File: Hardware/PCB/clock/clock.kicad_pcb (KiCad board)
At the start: 2 copper layers, 146 x 170.5 mm, 65 parts, among them J1 AudioJack2, J2 Synth_power_2x5, J3 AudioJack2, J4 AudioJack2, J5 AudioJack2, J6 AudioJack2, J7 AudioJack2, J8 Conn_02x04_Odd_Even, J9 Conn_02x04_Odd_Even, SW1 RotaryEncoder, SW2 SW_Push, U1 40106

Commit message: pre fab updates, gerbers, schem pdf
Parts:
- added B1: Board, ao_tht:Board_Marker, F.Cu at (96.5, 42.5)
- added B2: Board, ao_tht:Board_Marker, F.Cu at (171.5, 14.5)
- renumbered C4 to C1, C1 to C2, C2 to C3, C3 to C4, D2 to D1, D4 to D10, D5 to D11, D6 to D12, D7 to D13, D1 to D2, D8 to D3, D9 to D4, D10 to D5, D11 to D6, D12 to D7, D13 to D8, D3 to D9, H3 to H2, H2 to H3, J9 to J1, J8 to J3, J1 to J4, J3 to J5, J4 to J6, J5 to J7, J6 to J8, J7 to J9, R5 to R1, R12 to R10, R13 to R11, R14 to R12, R15 to R13, R16 to R14, R6 to R15, R17 to R16, R18 to R17, R19 to R18, R20 to R19, R10 to R2, R21 to R20, R2 to R3, R3 to R4, R4 to R5, R7 to R6, R8 to R7, R9 to R8, R1 to R9, SW2 to SW1, SW1 to SW2

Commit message: Fix wayward trace; add silk labels for LEDs and RLs
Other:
- board text added: "Green"
- board text added: "Red"
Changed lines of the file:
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@@
   (gr_line (start 57 65) (end 57 185) (layer "Edge.Cuts") (width 0.1))
   (gr_line (start 79 42.5) (end 79 65) (layer "Edge.Cuts") (width 0.1))
+  (gr_text "Green" (at 85.728 136.988) (layer "B.SilkS")
+    (effects (font (size 1 1) (thickness 0.15)) (justify mirror))
+  )
   (gr_text "GND" (at 179.842 24.384 90) (layer "B.SilkS")
     (effects (font (size 1 1) (thickness 0.15)) (justify mirror))
@@
     (effects (font (size 1 1) (thickness 0.15)) (justify mirror))
   )
+  (gr_text "Red" (at 74.552 112.604) (layer "B.SilkS")
+    (effects (font (size 1 1) (thickness 0.15)) (justify mirror))
+  )
   (gr_text "https://github.com/holmesrichards/clock" (at 101.61 73.66 90) (layer "B.SilkS")
     (effects (font (size 1 1) (thickness 0.15)) (justify mirror))
   )
+  (gr_text "Green" (at 85.728 162.388) (layer "B.SilkS")
+    (effects (font (size 1 1) (thickness 0.15)) (justify mirror))
+  )
+  (gr_text "Green" (at 85.725 112.604) (layer "B.SilkS")
+    (effects (font (size 1 1) (thickness 0.15)) (justify mirror))
+  )
+  (gr_text "Green" (at 74.044 162.388) (layer "B.SilkS")
+    (effects (font (size 1 1) (thickness 0.15)) (justify mirror))
+  )
   (gr_text "CLOCK\nRich Holmes\n7/2022 CC0 1.0" (at 70.495 78.74) (layer "B.SilkS")
+    (effects (font (size 1 1) (thickness 0.15)) (justify mirror))
+  )
+  (gr_text "Green" (at 74.295 136.988) (layer "B.SilkS")
     (effects (font (size 1 1) (thickness 0.15)) (justify mirror))
   )
@@
   (gr_text "Close jumpers as\nappropriate for\nOLED power" (at 176.286 28.448) (layer "B.SilkS")
     (effects (font (size 1 1) (thickness 0.15)) (justify mirror))
+  )
+  (gr_text "Green" (at 80 134) (layer "F.SilkS")
+    (effects (font (size 1 1) (thickness 0.15)))
+  )
+  (gr_text "Green" (at 79.995 184) (layer "F.SilkS")
+    (effects (font (size 1 1) (thickness 0.15)))
+  )
+  (gr_text "Green" (at 79.995 159) (layer "F.SilkS")
+    (effects (font (size 1 1) (thickness 0.15)))
+  )
+  (gr_text "Red" (at 80 124) (layer "F.SilkS")
+    (effects (font (size 1 1) (thickness 0.15)))
+  )
+  (gr_text "Green" (at 79.995 174) (layer "F.SilkS")
+    (effects (font (size 1 1) (thickness 0.15)))
+  )
+  (gr_text "Green" (at 80 149) (layer "F.SilkS")
+    (effects (font (size 1 1) (thickness 0.15)))
   )
   (segment (start 90.17 93.355) (end 98.435 85.09) (width 0.75) (layer "B.Cu") (net 2))
@@
   (segment (start 90.17 133.003293) (end 90.17 135.89) (width 0.25) (layer "F.Cu") (net 9))
   (segment (start 92.71 139.7) (end 89.535 139.7) (width 0.25) (layer "B.Cu") (net 9))
-  (segment (start 67.975969 112.679983) (end 68.511489 113.215503) (width 0.25) (layer "F.Cu") (net 10))
-  (segment (start 69.57452 142.947813) (end 69.57452 149.401227) (width 0.25) (layer "F.Cu") (net 10))
-  (segment (start 83.195 54.61) (end 79.362511 58.442489) (width 0.25) (layer "F.Cu") (net 10))
-  (segment (start 68.511489 113.215503) (end 68.51149 116.884783) (width 0.25) (layer "F.Cu") (net 10))
-  (segment (start 66.97597 132.238381) (end 68.425489 133.6879) (width 0.25) (layer "F.Cu") (net 10))
-  (segment (start 79.362511 58.442489) (end 79.362511 103.136489) (width 0.25) (layer "F.Cu") (net 10))
-  (segment (start 69.85 163.83) (end 70.485 164.465) (width 0.25) (layer "F.Cu") (net 10))
-  (segment (start 69.85 161.29) (end 69.85 163.83) (width 0.25) (layer "F.Cu") (net 10))
+  (segment (start 81.620489 64.768511) (end 79.362511 67.026489) (width 0.25) (layer "F.Cu") (net 10))
+  (segment (start 79.362511 103.136489) (end 73.279 109.22) (width 0.25) (layer "F.Cu") (net 10))
+  (segment (start 66.975969 130.56162) (end 66.97597 132.238381) (width 0.25) (layer "F.Cu") (net 10))
+  (segment (start 73.279 109.22) (end 68.270261 109.22) (width 0.25) (layer "F.Cu") (net 10))
+  (segment (start 68.51149 116.884783) (end 69.57452 117.947813) (width 0.25) (layer "F.Cu") (net 10))
   (segment (start 72.57452 158.56548) (end 69.85 161.29) (width 0.25) (layer "F.Cu") (net 10))
   (segment (start 68.270261 109.22) (end 67.975969 109.514292) (width 0.25) (layer "F.Cu") (net 10))
-  (segment (start 68.51149 116.884783) (end 69.57452 117.947813) (width 0.25) (layer "F.Cu") (net 10))
+  (segment (start 69.57452 127.963069) (end 66.975969 130.56162) (width 0.25) (layer "F.Cu") (net 10))
+  (segment (start 69.57452 149.401227) (end 72.57452 152.401227) (width 0.25) (layer "F.Cu") (net 10))
+  (segment (start 69.85 163.83) (end 70.485 164.465) (width 0.25) (layer "F.Cu") (net 10))
+  (segment (start 68.425489 133.6879) (end 68.425489 141.798782) (width 0.25) (layer "F.Cu") (net 10))
+  (segment (start 79.362511 67.026489) (end 79.362511 103.136489) (width 0.25) (layer "F.Cu") (net 10))
+  (segment (start 69.85 161.29) (end 69.85 163.83) (width 0.25) (layer "F.Cu") (net 10))
   (segment (start 72.57452 152.401227) (end 72.57452 158.56548) (width 0.25) (layer "F.Cu") (net 10))
+  (segment (start 67.975969 112.679983) (end 68.511489 113.215503) (width 0.25) (layer "F.Cu") (net 10))
+  (segment (start 67.975969 109.514292) (end 67.975969 112.679983) (width 0.25) (layer "F.Cu") (net 10))
+  (segment (start 83.195 54.61) (end 81.620489 56.184511) (width 0.25) (layer "F.Cu") (net 10))
+  (segment (start 81.620489 56.184511) (end 81.620489 64.768511) (width 0.25) (layer "F.Cu") (net 10))
   (segment (start 69.57452 117.947813) (end 69.57452 127.963069) (width 0.25) (layer "F.Cu") (net 10))
+  (segment (start 68.511489 113.215503) (end 68.51149 116.884783) (width 0.25) (layer "F.Cu") (net 10))
   (segment (start 68.425489 141.798782) (end 69.57452 142.947813) (width 0.25) (layer "F.Cu") (net 10))
-  (segment (start 66.975969 130.56162) (end 66.97597 132.238381) (width 0.25) (layer "F.Cu") (net 10))
-  (segment (start 69.57452 149.401227) (end 72.57452 152.401227) (width 0.25) (layer "F.Cu") (net 10))
-  (segment (start 69.57452 127.963069) (end 66.975969 130.56162) (width 0.25) (layer "F.Cu") (net 10))
-  (segment (start 68.425489 133.6879) (end 68.425489 141.798782) (width 0.25) (layer "F.Cu") (net 10))
-  (segment (start 79.362511 103.136489) (end 73.279 109.22) (width 0.25) (layer "F.Cu") (net 10))
-  (segment (start 67.975969 109.514292) (end 67.975969 112.679983) (width 0.25) (layer "F.Cu") (net 10))
-  (segment (start 73.279 109.22) (end 68.270261 109.22) (width 0.25) (layer "F.Cu") (net 10))
+  (segment (start 69.57452 142.947813) (end 69.57452 149.401227) (width 0.25) (layer "F.Cu") (net 10))
+  (segment (start 66.97597 132.238381) (end 68.425489 133.6879) (width 0.25) (layer "F.Cu") (net 10))
   (segment (start 67.31 164.465) (end 70.485 164.465) (width 0.25) (layer "B.Cu") (net 10))
   (segment (start 84.319511 53.194511) (end 84.319511 57.522511) (width 0.25) (layer "F.Cu") (net 11))

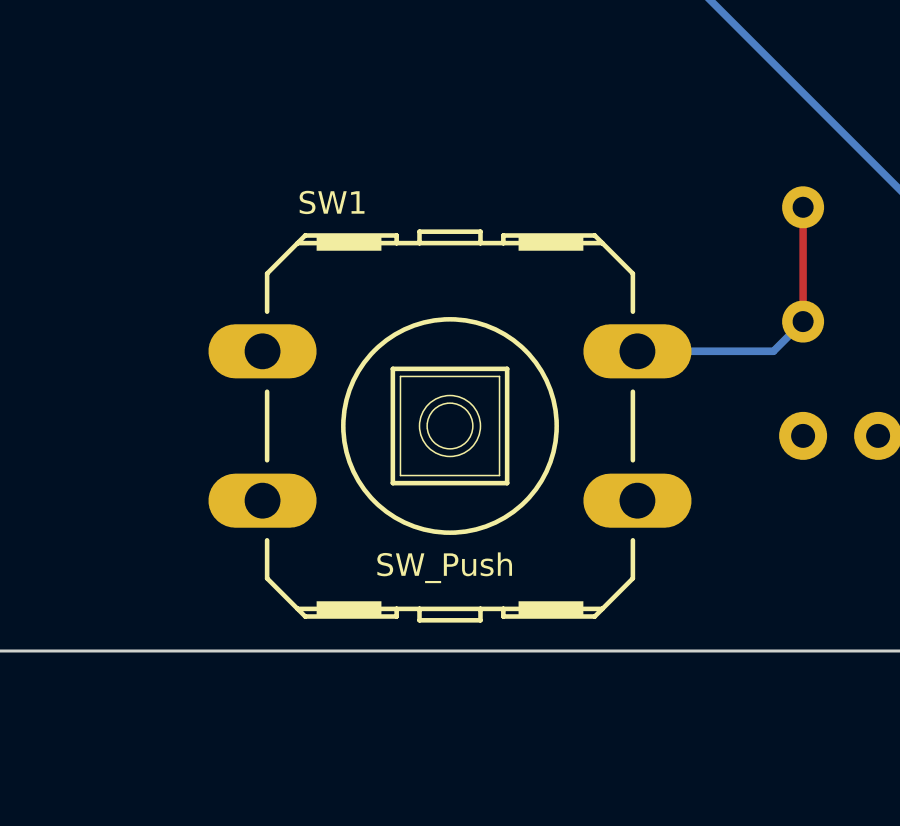
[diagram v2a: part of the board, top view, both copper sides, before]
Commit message: Correct switch footprint
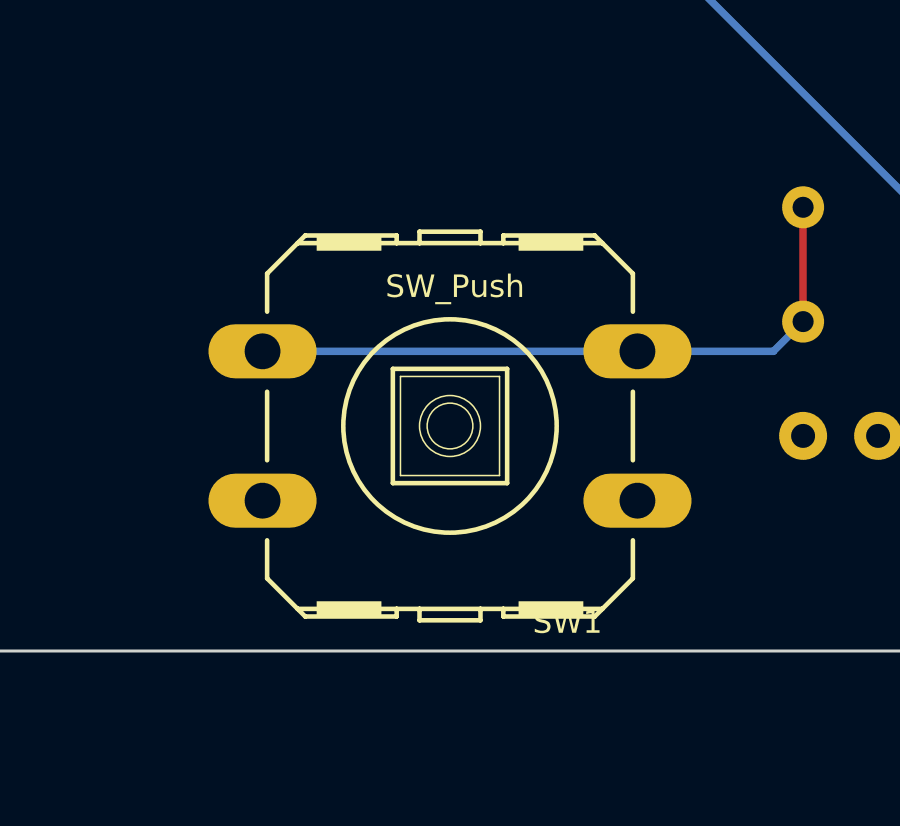
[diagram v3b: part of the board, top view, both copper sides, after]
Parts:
- turned SW1 to 180 degrees
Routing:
- net Net-(R1-Pad2): track 9.74 -> 22.2 mm
